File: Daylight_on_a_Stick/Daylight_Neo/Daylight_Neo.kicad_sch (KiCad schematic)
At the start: 30 parts

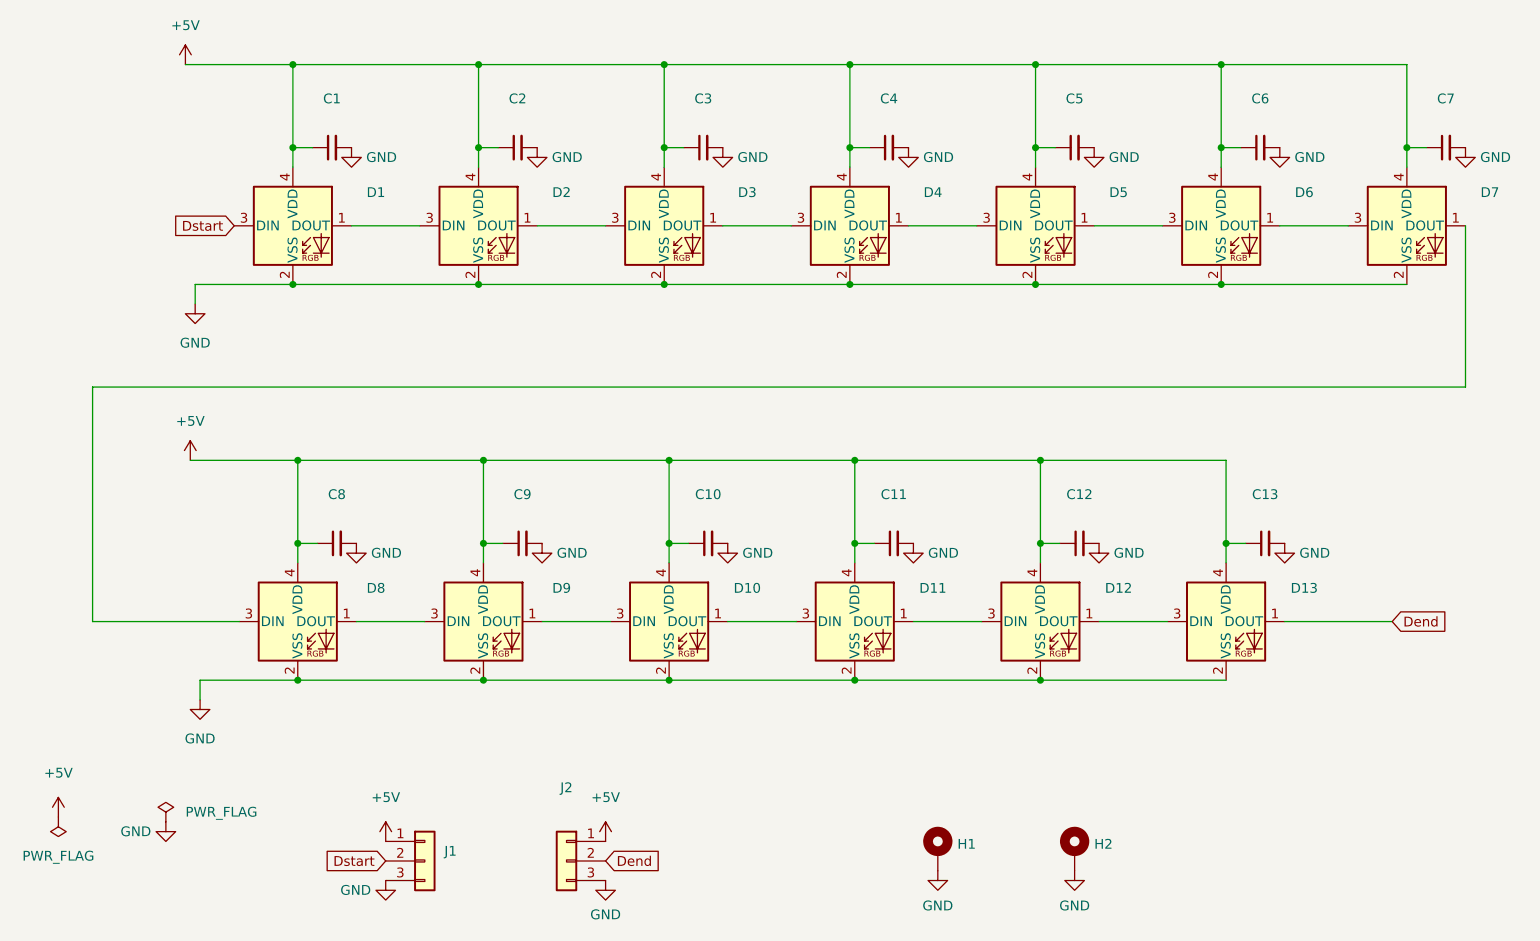
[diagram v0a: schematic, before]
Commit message: Fixed some Layout LED footprint issues
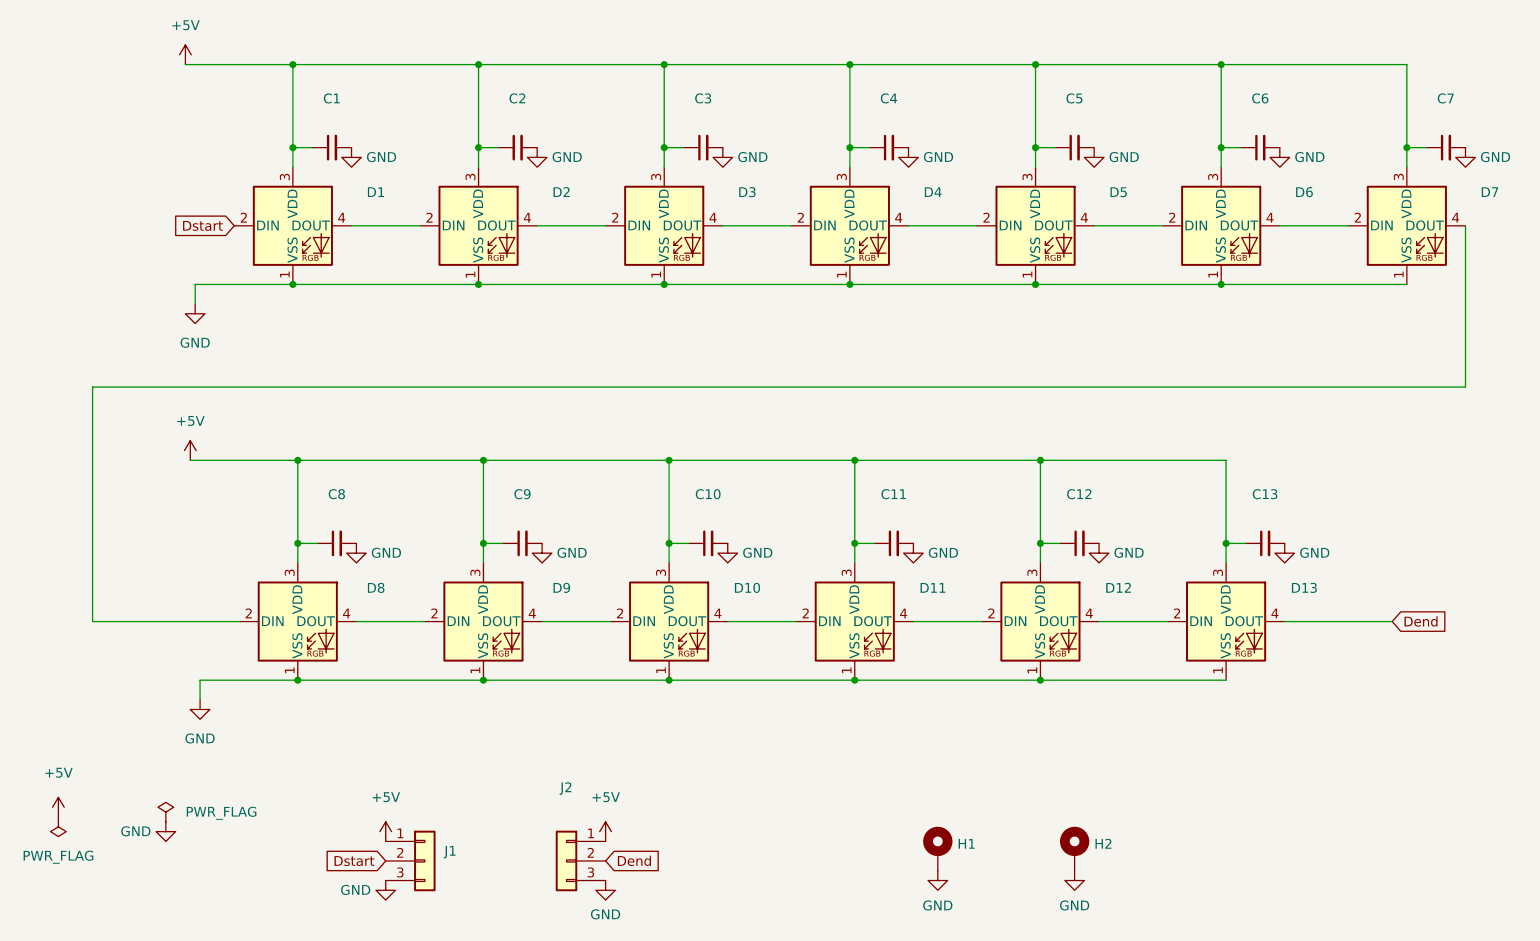
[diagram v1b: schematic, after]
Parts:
- C1, C10, C11, C12, C13, C2, C3, C4, C5, C6, C7, C8, C9: LCSC C24497 -> C28233
- D1, D10, D11, D12, D13, D2, D3, D4, D5, D6, D7, D8, D9: symbol LED:SK6812MINI -> LED:SK6812
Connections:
- net +5V: now also D1.3 (VDD), D10.3 (VDD), D11.3 (VDD), D12.3 (VDD), D13.3 (VDD), D2.3 (VDD), D3.3 (VDD), D4.3 (VDD), D5.3 (VDD), D6.3 (VDD), D7.3 (VDD), D8.3 (VDD), D9.3 (VDD); no longer D1.4 (VDD), D10.4 (VDD), D11.4 (VDD), D12.4 (VDD), D13.4 (VDD), D2.4 (VDD), D3.4 (VDD), D4.4 (VDD), D5.4 (VDD), D6.4 (VDD), D7.4 (VDD), D8.4 (VDD), D9.4 (VDD)
- net Dend: now also D13.4 (DOUT); no longer D13.1 (DOUT)
- net Dstart: now also D1.2 (DIN); no longer D1.3 (DIN)
- net GND: now also D1.1 (VSS), D10.1 (VSS), D11.1 (VSS), D12.1 (VSS), D13.1 (VSS), D2.1 (VSS), D3.1 (VSS), D4.1 (VSS), D5.1 (VSS), D6.1 (VSS), D7.1 (VSS), D8.1 (VSS), D9.1 (VSS); no longer D1.2 (VSS), D10.2 (VSS), D11.2 (VSS), D12.2 (VSS), D13.2 (VSS), D2.2 (VSS), D3.2 (VSS), D4.2 (VSS), D5.2 (VSS), D6.2 (VSS), D7.2 (VSS), D8.2 (VSS), D9.2 (VSS)
- new net: D10.4 (DOUT), D11.2 (DIN)
- new net: D11.4 (DOUT), D12.2 (DIN)
- new net: D2.4 (DOUT), D3.2 (DIN)
- new net: D3.4 (DOUT), D4.2 (DIN)
- new net: D1.4 (DOUT), D2.2 (DIN)
- new net: D4.4 (DOUT), D5.2 (DIN)
- new net: D12.4 (DOUT), D13.2 (DIN)
- new net: D5.4 (DOUT), D6.2 (DIN)
- new net: D6.4 (DOUT), D7.2 (DIN)
- new net: D10.2 (DIN), D9.4 (DOUT)
- new net: D7.4 (DOUT), D8.2 (DIN)
- new net: D8.4 (DOUT), D9.2 (DIN)

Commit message: Minor LED Updates
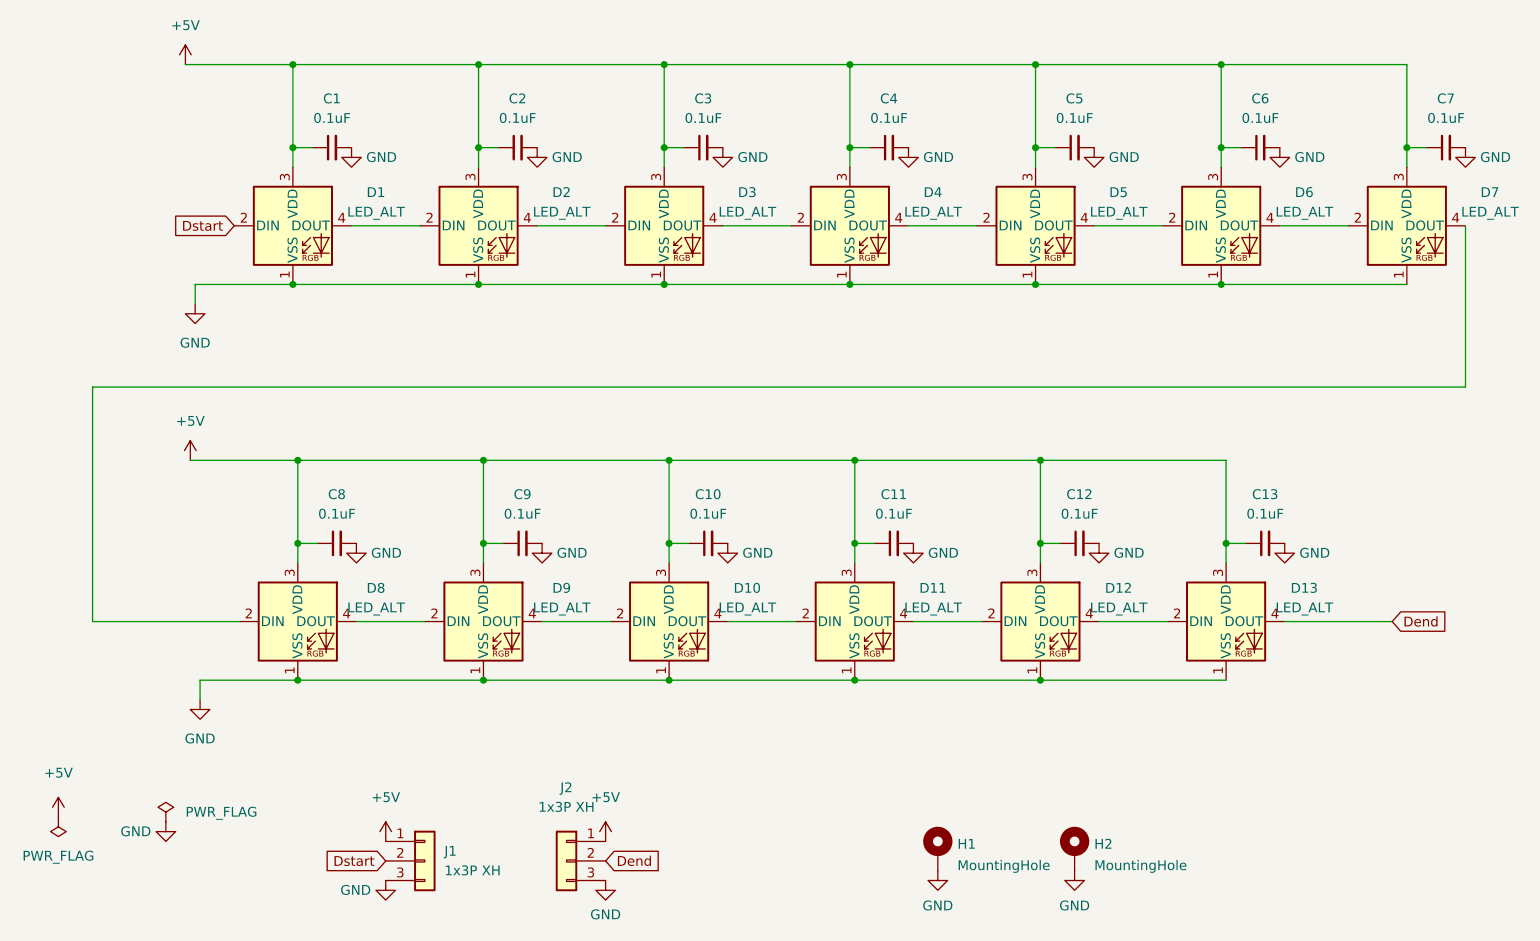
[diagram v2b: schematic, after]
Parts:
- C1, C10, C11, C12, C13, C2, C3, C4, C5, C6, C7, C8, C9: value (none) -> 0.1uF; footprint (none) -> Daylight:C_0805_2012Metric_Pad1.18x1.45mm_HandSolder_V3Dspec
- D1, D10, D11, D12, D13, D2, D3, D4, D5, D6, D7, D8, D9: value (none) -> LED_ALT; footprint (none) -> Daylight:XL-3528RGBW-WS2812B
- H1, H2: value (none) -> MountingHole; footprint (none) -> MountingHole:MountingHole_3.2mm_M3_Pad_Via
- J1, J2: value (none) -> 1x3P XH; footprint (none) -> Connector_JST:JST_XH_S3B-XH-A_1x03_P2.50mm_Horizontal; LCSC (none) -> C2908612
